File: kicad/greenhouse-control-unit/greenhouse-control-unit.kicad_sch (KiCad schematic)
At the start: 72 parts, among them J1 Pluggable_Terminal_01x02, J10 Molex_KK-254_01x10, J10_LittleBuck1 Conn_01x01_Female, J11_LittleBuck1 Conn_01x01_Female, J12_BigBuck1 Conn_01x01_Female, J13_BigBuck1 Conn_01x01_Female, J14_LittleBuck1 Conn_01x01_Female, J15_LittleBuck1 Conn_01x01_Female, J2 Pluggable_Terminal_01x02, J3 Pluggable_Terminal_01x02, J4 Molex_KK-254_01x08, J5 Conn_01x10_Female, J6 Conn_01x10_Female, J6_BigBuck1 Conn_01x01_Female, J7 Conn_01x15_Female, J7_BigBuck1 Conn_01x01_Female, J8 Conn_01x15_Female, J9 Molex_KK-396_01x16, Q1 2N7000, Q10 IRLB8721PBF, Q11 IRLB8721PBF, Q12 2N7000, Q13 2N7000, Q2 2N7000, Q3 2N7000, Q4 IRLB8721PBF, Q5 IRLB8721PBF, Q6 IRLB8721PBF, Q7 IRLB8721PBF, Q8 IRLB8721PBF, Q9 IRLB8721PBF, U1 74HC595, U2 74HC595

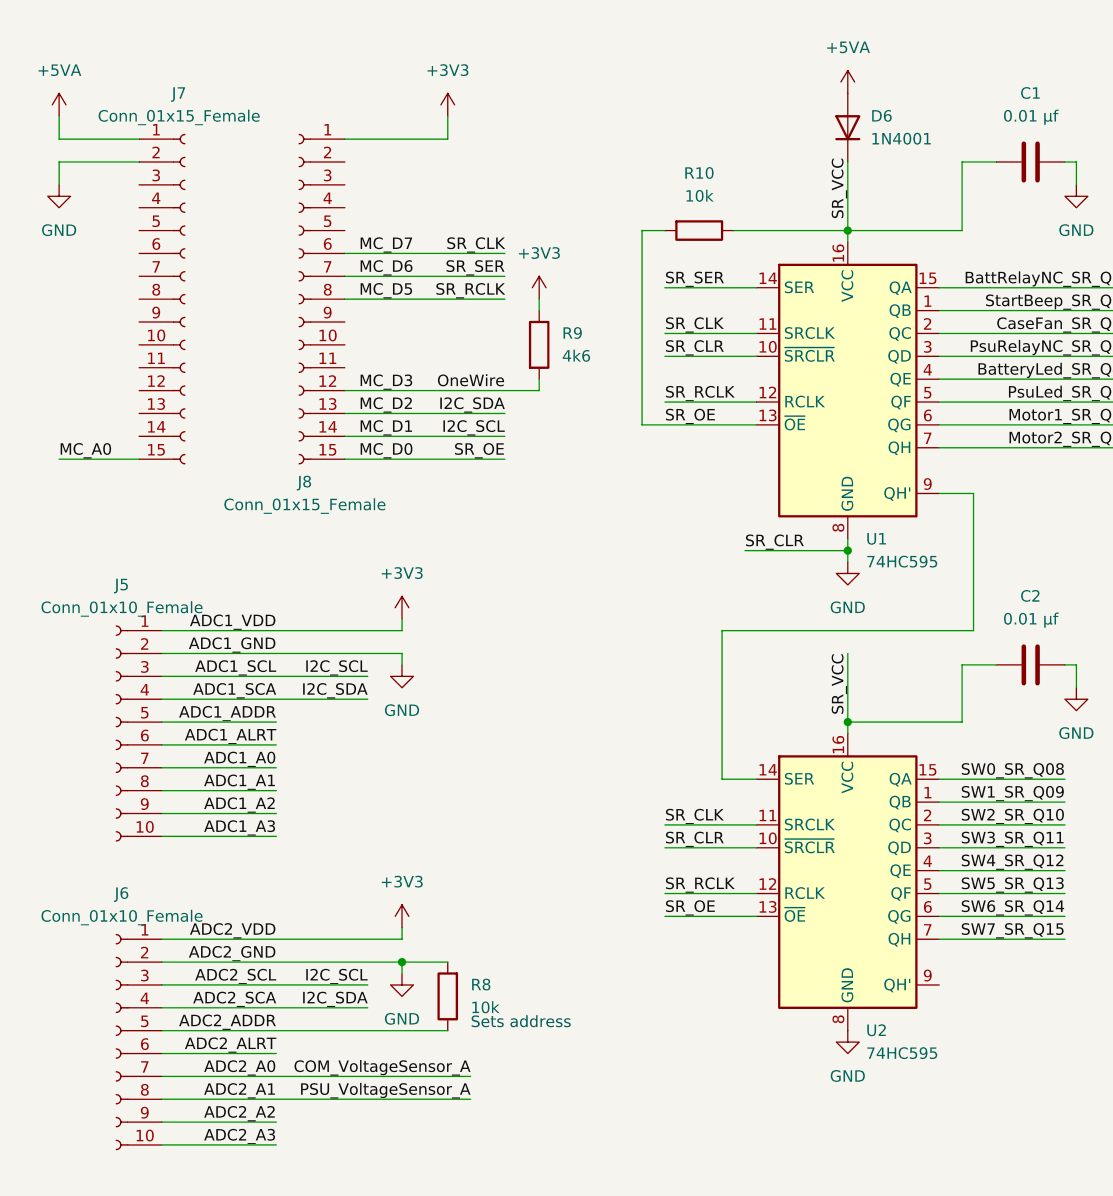
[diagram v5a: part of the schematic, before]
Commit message: SRCLR on SR must be high
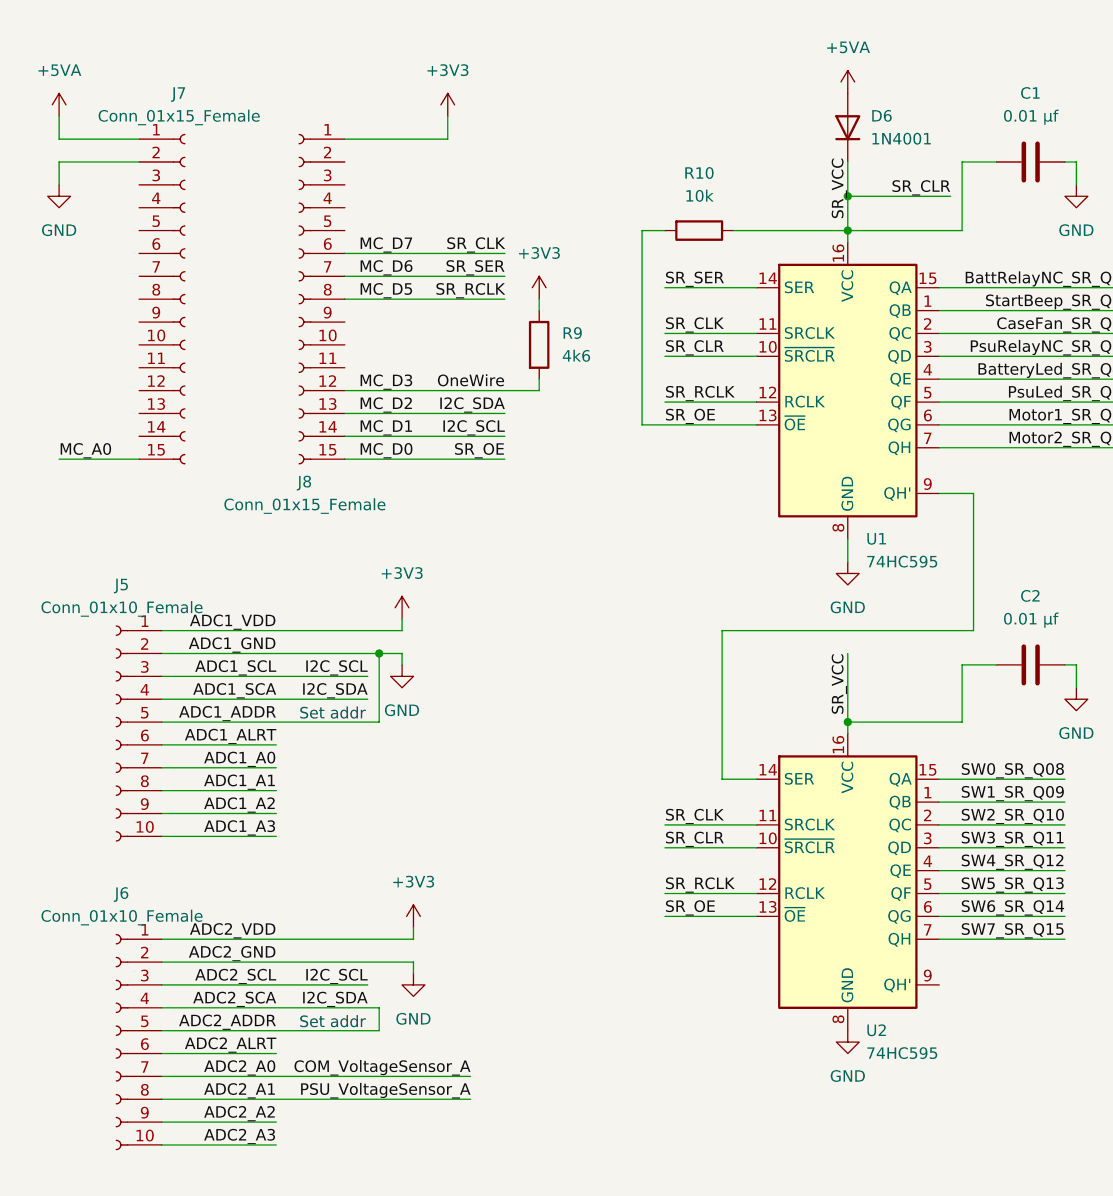
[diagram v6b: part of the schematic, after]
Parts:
- removed R8: 10k, Resistor_THT:R_Axial_DIN0204_L3.6mm_D1.6mm_P5.08mm_Horizontal, symbol Device:R
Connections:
- net ADC1_ADDR is gone; now on net GND: J5.5 (Pin_5)
- net ADC2_ADDR is gone; now on net ADC1_SCA: J6.5 (Pin_5)
- net GND: no longer U1.10 (~{SRCLR}), U2.10 (~{SRCLR})
- net SR_VCC renamed SR_CLR
- net SR_CLR: now also U1.10 (~{SRCLR}), U2.10 (~{SRCLR})
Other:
- note added: "Set addr"
- note removed: "Sets address"
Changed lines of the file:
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@@
   (junction (at 38.1 227.33) (diameter 0) (color 0 0 0 0)
   )
-  (junction (at 233.68 107.95) (diameter 0) (color 0 0 0 0)
-  )
   (junction (at 38.1 214.63) (diameter 0) (color 0 0 0 0)
   )
@@
   (junction (at 223.52 212.09) (diameter 0) (color 0 0 0 0)
   )
+  (junction (at 181.61 119.38) (diameter 0) (color 0 0 0 0)
+  )
   (junction (at 143.51 226.06) (diameter 0) (color 0 0 0 0)
   )
@@
   (junction (at 132.08 121.92) (diameter 0) (color 0 0 0 0)
   )
-  (junction (at 67.31 227.33) (diameter 0) (color 0 0 0 0)
+  (junction (at 233.68 68.58) (diameter 0) (color 0 0 0 0)
   )
-  (junction (at 184.15 153.67) (diameter 0) (color 0 0 0 0)
+  (junction (at 67.31 227.33) (diameter 0) (color 0 0 0 0)
   )
   (junction (at 132.08 114.3) (diameter 0) (color 0 0 0 0)
@@
   (junction (at 332.74 143.51) (diameter 0) (color 0 0 0 0)
   )
-  (wire (pts (xy 184.15 149.86) (xy 184.15 151.13))
+  (wire (pts (xy 185.42 149.86) (xy 185.42 151.13))
     (stroke (width 0) (type default) (color 0 0 0 0))
   )
@@
     (stroke (width 0) (type default) (color 0 0 0 0))
   )
+  (wire (pts (xy 233.68 68.58) (xy 233.68 72.39))
+    (stroke (width 0) (type default) (color 0 0 0 0))
+  )
   (wire (pts (xy 71.12 58.42) (xy 71.12 69.85))
     (stroke (width 0) (type default) (color 0 0 0 0))
@@
     (stroke (width 0) (type default) (color 0 0 0 0))
   )
-  (wire (pts (xy 222.25 107.95) (xy 233.68 107.95))
-    (stroke (width 0) (type default) (color 0 0 0 0))
-  )
   (wire (pts (xy 247.65 116.84) (xy 219.71 116.84))
     (stroke (width 0) (type default) (color 0 0 0 0))
@@
     (stroke (width 0) (type default) (color 0 0 0 0))
   )
-  (wire (pts (xy 233.68 109.22) (xy 233.68 107.95))
+  (wire (pts (xy 233.68 106.68) (xy 233.68 109.22))
     (stroke (width 0) (type default) (color 0 0 0 0))
   )
@@
     (stroke (width 0) (type default) (color 0 0 0 0))
   )
-  (wire (pts (xy 157.48 119.38) (xy 184.15 119.38))
+  (wire (pts (xy 157.48 119.38) (xy 181.61 119.38))
     (stroke (width 0) (type default) (color 0 0 0 0))
   )
@@
     (stroke (width 0) (type default) (color 0 0 0 0))
   )
-  (wire (pts (xy 157.48 161.29) (xy 189.23 161.29))
+  (wire (pts (xy 157.48 161.29) (xy 181.61 161.29))
     (stroke (width 0) (type default) (color 0 0 0 0))
   )
@@
     (stroke (width 0) (type default) (color 0 0 0 0))
   )
-  (wire (pts (xy 157.48 127) (xy 170.18 127))
+  (wire (pts (xy 157.48 127) (xy 181.61 127))
     (stroke (width 0) (type default) (color 0 0 0 0))
   )
@@
     (stroke (width 0) (type default) (color 0 0 0 0))
   )
-  (wire (pts (xy 233.68 64.77) (xy 233.68 72.39))
+  (wire (pts (xy 233.68 64.77) (xy 233.68 68.58))
     (stroke (width 0) (type default) (color 0 0 0 0))
   )
@@
     (stroke (width 0) (type default) (color 0 0 0 0))
   )
-  (wire (pts (xy 184.15 153.67) (xy 189.23 153.67))
-    (stroke (width 0) (type default) (color 0 0 0 0))
-  )
   (wire (pts (xy 308.61 209.55) (xy 293.37 209.55))
     (stroke (width 0) (type default) (color 0 0 0 0))
@@
     (stroke (width 0) (type default) (color 0 0 0 0))
   )
-  (wire (pts (xy 233.68 107.95) (xy 233.68 106.68))
+  (wire (pts (xy 245.11 68.58) (xy 233.68 68.58))
     (stroke (width 0) (type default) (color 0 0 0 0))
   )
@@
     (stroke (width 0) (type default) (color 0 0 0 0))
   )
+  (wire (pts (xy 181.61 119.38) (xy 184.15 119.38))
+    (stroke (width 0) (type default) (color 0 0 0 0))
+  )
   (wire (pts (xy 213.36 72.39) (xy 210.82 72.39))
     (stroke (width 0) (type default) (color 0 0 0 0))
@@
     (stroke (width 0) (type default) (color 0 0 0 0))
   )
-  (wire (pts (xy 157.48 151.13) (xy 184.15 151.13))
+  (wire (pts (xy 157.48 151.13) (xy 185.42 151.13))
     (stroke (width 0) (type default) (color 0 0 0 0))
   )
@@
     (stroke (width 0) (type default) (color 0 0 0 0))
   )
+  (wire (pts (xy 157.48 156.21) (xy 180.34 156.21))
+    (stroke (width 0) (type default) (color 0 0 0 0))
+  )
   (wire (pts (xy 368.3 110.49) (xy 378.46 110.49))
     (stroke (width 0) (type default) (color 0 0 0 0))
   )
+  (wire (pts (xy 181.61 127) (xy 181.61 119.38))
+    (stroke (width 0) (type default) (color 0 0 0 0))
+  )
   (wire (pts (xy 154.94 64.77) (xy 146.05 64.77))
     (stroke (width 0) (type default) (color 0 0 0 0))
@@
     (stroke (width 0) (type default) (color 0 0 0 0))
   )
+  (wire (pts (xy 181.61 158.75) (xy 181.61 161.29))
+    (stroke (width 0) (type default) (color 0 0 0 0))
+  )
   (wire (pts (xy 38.1 237.49) (xy 38.1 238.76))
     (stroke (width 0) (type default) (color 0 0 0 0))
@@
     (stroke (width 0) (type default) (color 0 0 0 0))
   )
-  (wire (pts (xy 157.48 158.75) (xy 180.34 158.75))
+  (wire (pts (xy 157.48 158.75) (xy 181.61 158.75))
     (stroke (width 0) (type default) (color 0 0 0 0))
   )
@@
     (stroke (width 0) (type default) (color 0 0 0 0))
   )
-  (wire (pts (xy 184.15 154.94) (xy 184.15 153.67))
+  (wire (pts (xy 185.42 154.94) (xy 185.42 153.67))
     (stroke (width 0) (type default) (color 0 0 0 0))
   )
@@
     (stroke (width 0) (type default) (color 0 0 0 0))
   )
-  (wire (pts (xy 157.48 156.21) (xy 180.34 156.21))
-    (stroke (width 0) (type default) (color 0 0 0 0))
-  )
   (wire (pts (xy 177.8 80.01) (xy 195.58 80.01))
     (stroke (width 0) (type default) (color 0 0 0 0))
@@
     (stroke (width 0) (type default) (color 0 0 0 0))
   )
-  (wire (pts (xy 157.48 153.67) (xy 184.15 153.67))
+  (wire (pts (xy 157.48 153.67) (xy 185.42 153.67))
     (stroke (width 0) (type default) (color 0 0 0 0))
   )
@@
     (effects (font (size 1.27 1.27)) (justify left bottom))
   )
-  (text "Sets address" (at 191.77 161.29 0)
+  (text "Set addr" (at 172.72 127 0)
+    (effects (font (size 1.27 1.27)) (justify left bottom))
+  )
+  (text "Set addr" (at 172.72 161.29 0)
     (effects (font (size 1.27 1.27)) (justify left bottom))
   )
@@
     (effects (font (size 1.27 1.27)) (justify left bottom))
   )
-  (label "SR_CLR" (at 222.25 107.95 0)
-    (effects (font (size 1.27 1.27)) (justify left bottom))
-  )
   (label "OUT+5V" (at 109.22 143.51 180)
     (effects (font (size 1.27 1.27)) (justify right bottom))
@@
     (effects (font (size 1.27 1.27)) (justify left bottom))
   )
+  (label "SR_CLR" (at 245.11 68.58 180)
+    (effects (font (size 1.27 1.27)) (justify right bottom))
+  )
   (label "SW3_SR_Q11" (at 257.81 140.97 180)
     (effects (font (size 1.27 1.27)) (justify right bottom))
@@
     (pin "1")
   )
-  (symbol (lib_id "power:+3V3") (at 184.15 149.86 0) (unit 1)
+  (symbol (lib_id "power:+3V3") (at 185.42 149.86 0) (unit 1)
     (in_bom yes) (on_board yes) (fields_autoplaced)
-    (property "Reference" "#PWR019" (id 0) (at 184.15 153.67 0)
+    (property "Reference" "#PWR019" (id 0) (at 185.42 153.67 0)
       (effects (font (size 1.27 1.27)) hide)
     )
-    (property "Value" "+3V3" (id 1) (at 184.15 144.78 0))
-    (property "Footprint" "" (id 2) (at 184.15 149.86 0)
+    (property "Value" "+3V3" (id 1) (at 185.42 144.78 0))
+    (property "Footprint" "" (id 2) (at 185.42 149.86 0)
       (effects (font (size 1.27 1.27)) hide)
     )
-    (property "Datasheet" "" (id 3) (at 184.15 149.86 0)
+    (property "Datasheet" "" (id 3) (at 185.42 149.86 0)
       (effects (font (size 1.27 1.27)) hide)
     )
@@
     (pin "2")
   )
-  (symbol (lib_id "power:GND") (at 184.15 154.94 0) (unit 1)
+  (symbol (lib_id "power:GND") (at 185.42 154.94 0) (unit 1)
     (in_bom yes) (on_board yes) (fields_autoplaced)
-    (property "Reference" "#PWR020" (id 0) (at 184.15 161.29 0)
+    (property "Reference" "#PWR020" (id 0) (at 185.42 161.29 0)
       (effects (font (size 1.27 1.27)) hide)
     )
-    (property "Value" "GND" (id 1) (at 184.15 160.02 0))
-    (property "Footprint" "" (id 2) (at 184.15 154.94 0)
+    (property "Value" "GND" (id 1) (at 185.42 160.02 0))
+    (property "Footprint" "" (id 2) (at 185.42 154.94 0)
       (effects (font (size 1.27 1.27)) hide)
     )
-    (property "Datasheet" "" (id 3) (at 184.15 154.94 0)
+    (property "Datasheet" "" (id 3) (at 185.42 154.94 0)
       (effects (font (size 1.27 1.27)) hide)
     )
@@
     (pin "1")
   )
-  (symbol (lib_id "Device:R") (at 189.23 157.48 180) (unit 1)
-    (in_bom yes) (on_board yes) (fields_autoplaced)
-    (property "Reference" "R8" (id 0) (at 191.77 156.2099 0)
-      (effects (font (size 1.27 1.27)) (justify right))
-    )
-    (property "Value" "10k" (id 1) (at 191.77 158.7499 0)
-      (effects (font (size 1.27 1.27)) (justify right))
-    )
-    (property "Footprint" "Resistor_THT:R_Axial_DIN0204_L3.6mm_D1.6mm_P5.08mm_Horizontal" (id 2) (at 191.008 157.48 90)
-      (effects (font (size 1.27 1.27)) hide)
-    )
-    (property "Datasheet" "~" (id 3) (at 189.23 157.48 0)
-      (effects (font (size 1.27 1.27)) hide)
-    )
-    (pin "1")
-    (pin "2")
-  )
   (symbol (lib_id "power:+12V") (at 132.08 69.85 0) (unit 1)
     (in_bom yes) (on_board yes) (fields_autoplaced)
@@
       (reference "R7") (unit 1) (value "2k") (footprint "Resistor_THT:R_Axial_DIN0207_L6.3mm_D2.5mm_P7.62mm_Horizontal")
     )
-    (path "/7b61dcda-89df-4fb3-8e4e-9b73486faf45"
-      (reference "R8") (unit 1) (value "10k") (footprint "Resistor_THT:R_Axial_DIN0204_L3.6mm_D1.6mm_P5.08mm_Horizontal")
-    )
     (path "/48f1e3b1-710a-42d1-bfff-ca44e51fda44"

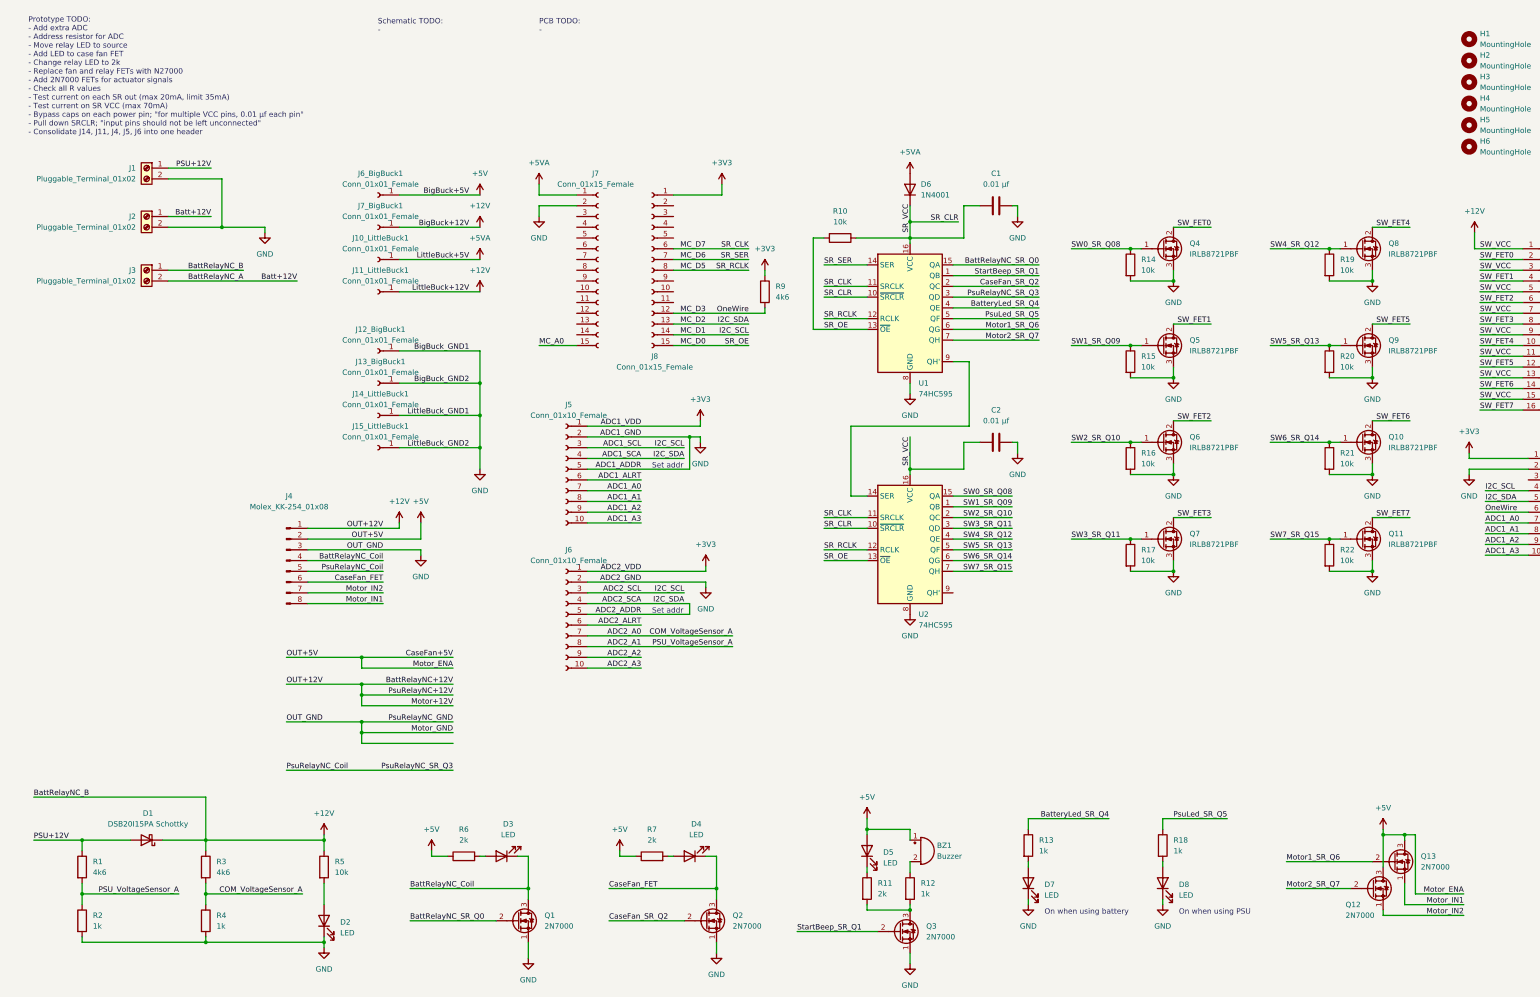
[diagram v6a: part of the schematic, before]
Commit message: Remove FETs for motor controller; not needed if EN is 5V
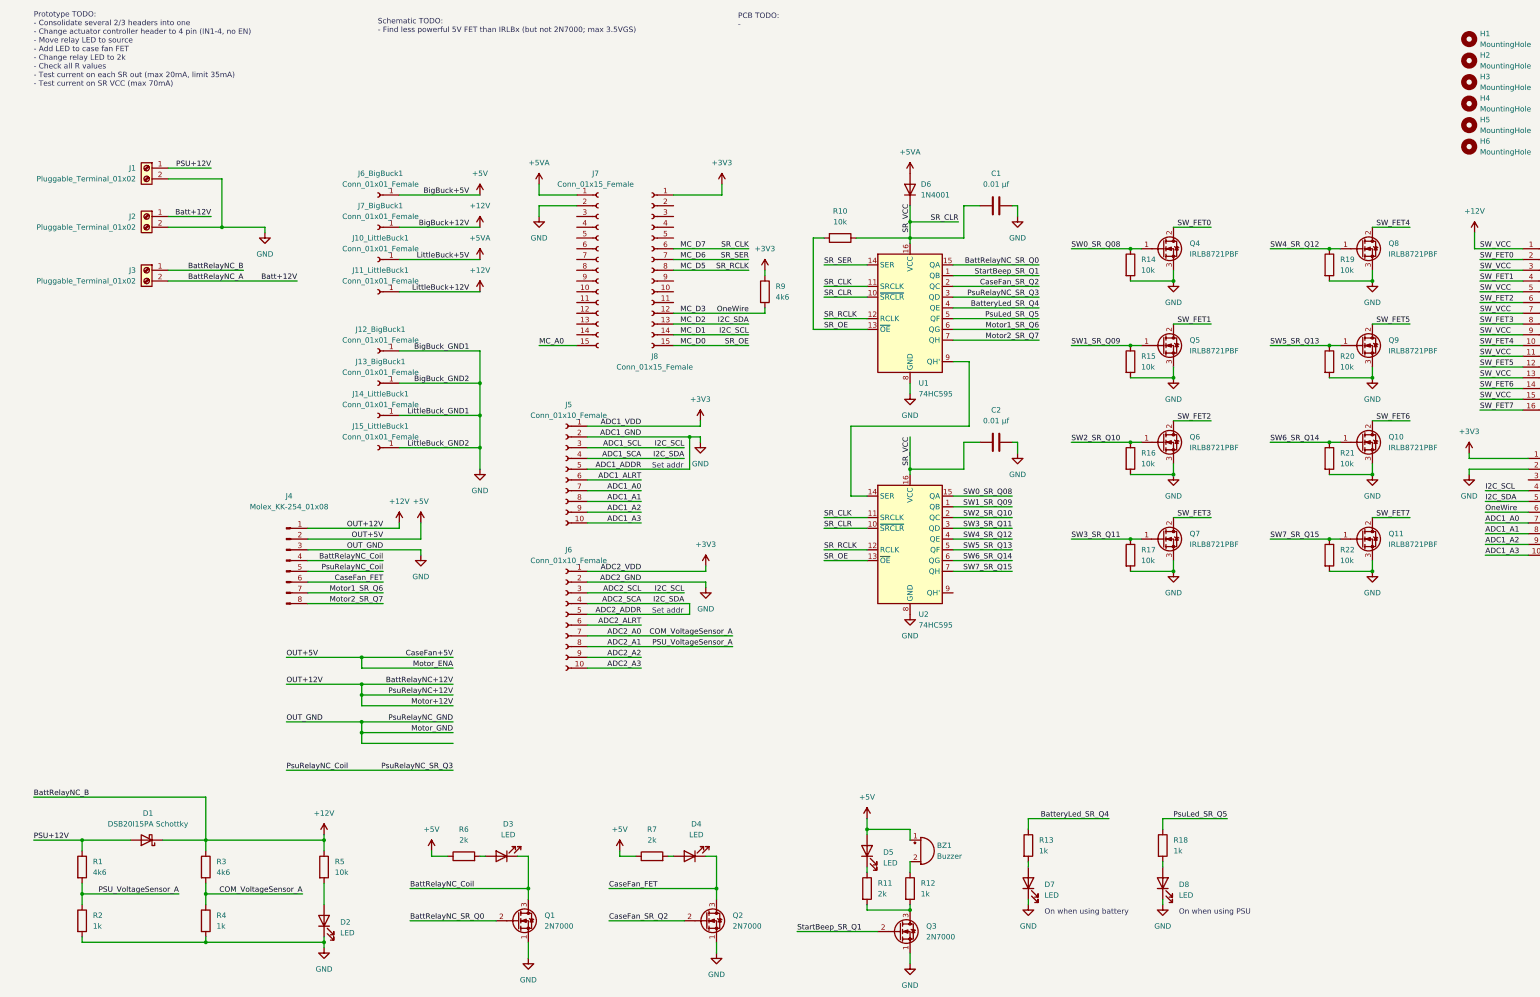
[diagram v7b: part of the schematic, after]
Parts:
- removed Q12, Q13: 2N7000, Package_TO_SOT_THT:TO-92_Inline, symbol Transistor_FET:2N7000
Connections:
- net Motor_IN1 is gone; now on net Motor2_SR_Q7: J4.8 (Pin_8)
- net Motor_IN2 is gone; now on net Motor1_SR_Q6: J4.7 (Pin_7)
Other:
- note added: "Prototype TODO: - Consolidate several 2/3 headers into one - Change actuator controller header to 4 pin (IN1-4, no EN) - Move relay LED to source - Add LED to case fan FET - Change relay LED to 2k - Check all R values - Test current on each SR out (max 20mA, limit 35mA) - Test current on SR VCC (max 70mA)"
- note added: "Schematic TODO: - Find less powerful 5V FET than IRLBx (but not 2N7000; max 3.5VGS)"
- note removed: "Prototype TODO: - Add extra ADC - Address resistor for ADC - Move relay LED to source - Add LED to case fan FET - Change relay LED to 2k - Replace fan and relay FETs with N27000 - Add 2N7000 FETs for actuator signals - Check all R values - Test current on each SR out (max 20mA, limit 35mA) - Test current on SR VCC (max 70mA) - Bypass caps on each power pin; "for multiple VCC pins, 0.01 μf each pi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"
- note removed: "Schematic TODO: -"
